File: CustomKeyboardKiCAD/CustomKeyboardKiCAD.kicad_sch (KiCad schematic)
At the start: 4 parts, among them J1 USB_C_Receptacle_USB2.0_16P, U1 nRF52840

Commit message: Progress on schematic
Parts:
- added C1: 10uF, symbol Device:C
- added C2, C3: 4.7uF, symbol Device:C
- added D1: BLUE, symbol Device:D
- added R3: 1K, symbol Device:R
- added R4: 10M, symbol Device:R
- added U2: XC6220B331MR, Package_TO_SOT_SMD:SOT-23-5, symbol Regulator_Linear:XC6220B331MR
- added U4: BQ24075RGTR, BQ24075RGTR:QFN50P300X300X100-17N, symbol BQ24075RGTR:BQ24075RGTR
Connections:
- net GND: now also C1.1, C2.1, R3.2, U2.2 (GND), U4.15 (SYSOFF), U4.17 (EXP), U4.4 (~{CE}), U4.5 (EN2), U4.8 (VSS)
- new net: D1.1 (K), R3.1
- new net BLED: D1.2 (A)
- new net EXT_VCC: C2.2, U2.5 (VOUT)
- new net POWER_PIN: R4.2, U2.3 (CE)
- new net VDDH: C1.2, R4.1, U2.1 (VIN), U4.6 (EN1)
- no-connect marks 3 -> 5
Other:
- moved on the sheet: J1, R1, R2

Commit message: updated the schematic
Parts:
- added C10, C17, C18, C19: 100nF, symbol Device:C
- added C11: 100pF, symbol Device:C
- added C12: 820pF, symbol Device:C
- added C13, C14, C15, C16, C5: 4.7uF, symbol Device:C
- added C20, C4, C8: 1uF, symbol Device:C
- added C21, C22, C6, C7: 12pF, symbol Device:C
- added C23, C24: 1pF, symbol Device:C
- added C25: 1.5pF, symbol Device:C
- added C26, C27, C28: 0.1uF, symbol Device:C
- added C9: 47nF, symbol Device:C
- added D2: ORANGE, symbol Device:LED
- added J2, J3: Conn_01x12_Pin, symbol Connector:Conn_01x12_Pin
- added JP1: Charge Boost, symbol Jumper:Jumper_2_Open
- added L1, L2: 10uH, symbol Device:L
- added L3: 15uH, symbol Device:L
- added L4: 3.9nH, symbol Device:L
- added R5, R6, R7: 10k, symbol Device:R
- added R8: 2k, symbol Device:R
- added R9: 0, symbol Device:R
- added U3, U5, U6: 74HC595, symbol 74xx:74HC595
- added Y1: 32.768kHz FC-12M, symbol Device:Crystal
- added Y2: 32MHz XRCGB32MOODF1H5ORO, symbol Device:Crystal_GND2
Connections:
- net BLED: now also U1.AD10 (P0.15)
- net D+: now also U1.AD6 (D+)
- net D-: now also U1.AD4 (D-)
- net EXT_VCC: now also C26.2, C27.2, C28.2, U3.10 (~{SRCLR}), U3.16 (VCC), U5.10 (~{SRCLR}), U5.16 (VCC), U6.10 (~{SRCLR}), U6.16 (VCC)
- net GND: now also C3.2, U1.B7 (VSS), U1.EP (VSS), C10.2, C11.2, C12.2, C13.2, C14.2, C15.2, C16.2, C17.2, C18.2, C19.2, C20.2, C21.2, C22.2, C24.2, C25.2, C26.1, C27.1, C28.1, C4.2, C5.2, C6.2, C7.2, C8.2, C9.2, R6.1, R7.2, R8.2, U3.13 (~{OE}), U3.8 (GND), U5.13 (~{OE}), U5.8 (GND), U6.13 (~{OE}), U6.8 (GND), Y2.2
- net POWER_PIN: now also U1.AD8 (P0.13)
- net VBUS: now also U1.AD2 (VBUS), U4.13 (IN), C15.1, C4.1
- net VDDH: now also C3.1, U1.Y2 (VDDH), U4.10 (OUT_10), U4.11 (OUT_11), C14.1, R5.2
- net 029: now reaches U1.A10 (AIN5/P0.29)
- net 002: now reaches U1.A12 (AIN0/P0.02)
- net 115: now reaches U1.A14 (P1.15)
- net 113: now reaches U1.A16 (P1.13)
- net VDD_NRF: now reaches U1.A22 (VDD), U1.AD14 (VDD), U1.AD23 (VDD), U1.B1 (VDD), U1.W1 (VDD)
- net VDD_NRF: now also C16.1, C17.1, C18.1, C19.1, C20.1, L1.2
- net at U1.A23 (XC2): now also C21.1, Y2.3
- net 031: now reaches U1.A8 (AIN7/P0.31)
- net SWC: now reaches U1.AA24 (SWDCLK)
- net at U1.AB2 (DCCH): now also L1.1
- net RESET: now reaches U1.AC11 (P0.16)
- net RESET: now also U1.AC13 (P0.18/~{RESET}), U1.AC9 (P0.14)
- net SWD: now reaches U1.AC24 (SWDIO)
- net at U1.AC5 (DECUSB): now also C13.1
- net 017: now reaches U1.AD12 (P0.17)
- net 017: now also U3.12 (RCLK), U5.12 (RCLK), U6.12 (RCLK)
- net 020: now reaches U1.AD16 (P0.20)
- net 022: now reaches U1.AD18 (P0.22)
- net 024: now reaches U1.AD20 (P0.24)
- net 100: now reaches U1.AD22 (TRACEDATA0/P1.00)
- net 111: now reaches U1.B19 (P1.11)
- net at U1.B24 (XC1): now also C22.1, Y2.1
- net at U1.B3 (DCC): now also L2.2
- net at U1.B5 (DEC4): now also U1.E24 (DEC6), C8.1, C9.1, L3.1
- net at U1.C1 (DEC1): now also C10.1
- net at U1.D2 (XL1/P0.00): now also C7.1, Y1.2
- net at U1.D23 (DEC3): now also C11.1
- net at U1.F2 (XL2/P0.01): now also C6.1, Y1.1
- net VSS_PA: now reaches U1.F23 (VSS_PA)
- net VSS_PA: now also C23.2
- net 026: now reaches U1.G1 (P0.26)
- net at U1.H23 (ANT): now also C23.1, L4.2
- net 010: now reaches U1.J24 (NFC2/P0.10)
- net TXD: now reaches U1.L1 (P0.06)
- net 009: now reaches U1.L24 (NFC1/P0.09)
- net 008: now reaches U1.N1 (P0.08)
- net 008: now also U3.11 (SRCLK), U5.11 (SRCLK), U6.11 (SRCLK)
- net at U1.N24 (DEC5): now also C12.1
- net 107: now reaches U1.P23 (P1.07)
- net 106: now reaches U1.R24 (P1.06)
- net 106: now also U3.14 (SER)
- net 011: now reaches U1.T2 (TRACEDATA2/P0.11)
- net 012: now reaches U1.U1 (TRACEDATA1/P0.12)
- net 104: now reaches U1.U24 (P1.04)
- net 102: now reaches U1.W24 (P1.02)
- net 101: now reaches U1.Y23 (P1.01)
- net at U4.1 (TS): now also R6.2
- net at U4.16 (ISET): now also JP1.1 (A), R7.1
- net VBAT: now reaches U4.2 (BAT_2)
- net VBAT: now also U4.3 (BAT_3), C5.1
- net at U4.9 (~{CHG}): now also D2.1 (K)
- new net: D2.2 (A), R5.1
- new net: JP1.2 (B), R8.1
- new net: U3.9 (QH'), U5.14 (SER)
- new net: U5.9 (QH'), U6.14 (SER)
- new net: L2.1, L3.2
- new net: C24.1, L4.1, R9.2
- new net ANTENNA: C25.1, R9.1
- new net COL0: U3.15 (QA)
- new net COL1: U3.1 (QB)
- new net COL10: U5.2 (QC)
- new net COL11: U5.3 (QD)
- new net COL12: U5.4 (QE)
- new net COL13: U5.5 (QF)
- new net COL14: U5.6 (QG)
- new net COL15: U5.7 (QH)
- new net COL16: U6.15 (QA)
- new net COL17: U6.1 (QB)
- new net COL2: U3.2 (QC)
- new net COL3: U3.3 (QD)
- new net COL4: U3.4 (QE)
- new net COL5: U3.5 (QF)
- new net COL6: U3.6 (QG)
- new net COL7: U3.7 (QH)
- new net COL8: U5.15 (QA)
- new net COL9: U5.1 (QB)
- no-connect marks 5 -> 14
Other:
- moved on the sheet: C1, C2, C3, D1, J1, R1, R2, R3, R4, U2, U4

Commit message: major progress on schematic
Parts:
- removed J2, J3: Conn_01x12_Pin, symbol Connector:Conn_01x12_Pin
- added J3: S2B-PH-K-SLFSN, S2B-PH-K-S:CONN_S2B-PH-K-S_JST, symbol S2B-PH-K-S:S2B-PH-K-SLFSN
- added SW91: RotaryEncoder_Switch, Rotary_Encoder:RotaryEncoder_Alps_EC11E-Switch_Vertical_H20mm, symbol Device:RotaryEncoder_Switch
- added U7: nice_nano, nicenano:nice_nano, symbol nicenano:nice_nano
- U3: footprint (none) -> 74HC595D:SOP127P600X175-16N
- U5, U6: footprint (none) -> BQ24075RGTR:QFN50P300X300X100-17N
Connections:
- net 002: now also SW91.S1, U7.18 (AIN0/P0.02)
- net 008: now also U7.2 (RX1/P0.08)
- net 009: now also U7.13 (NFC1/P0.09)
- net 010: now also U7.14 (NFC2/P0.10)
- net 011: now also U7.10 (P0.11)
- net 017: now also U7.5 (P0.17)
- net 020: now also U7.6 (P0.20)
- net 022: now also U7.7 (P0.22)
- net 024: now also U7.8 (P0.24)
- net 029: now also SW91.C, U7.19 (AIN5/P0.29)
- net 031: now also SW91.A, U7.20 (AIN7/P0.31)
- net 100: now also U7.9 (P1.00)
- net 101: now also U7.31 (P1.01)
- net 102: now also U7.32 (P1.02)
- net 104: now also U7.11 (P1.04)
- net 106: now also U7.12 (P1.06)
- net 107: now also U7.33 (P1.07)
- net 111: now also U7.15 (P1.11)
- net 113: now also U7.16 (P1.13)
- net 115: now also U7.17 (P1.15)
- net EXT_VCC: now also U7.21 (VCC)
- net GND: now also J3.2, SW91.B, SW91.S2, U7.23 (GND), U7.3 (GND), U7.4 (GND)
- net RESET: now also U7.22 (RST)
- net VBAT: now also J3.1, U7.24 (BATIN/P0.04)
- net COL18: now reaches U6.2 (QC)
- net TXD renamed 006
- net 006: now also U7.1 (TX0/P0.06)
- no-connect marks 14 -> 31
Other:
- added sheet LEDs (LEDs.kicad_sch)
- added sheet keyboard_matrix (keyboard_matrix.kicad_sch)
- moved on the sheet: C26, C27, C28, U3, U5, U6

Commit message: schematic is generally complete
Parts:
- added J2: Display Connector, Connector_PinHeader_2.54mm:PinHeader_1x04_P2.54mm_Vertical, symbol Connector_Generic:Conn_01x04
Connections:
- net 010: now also J2.4 (Pin_4)
- net 111: now also J2.3 (Pin_3)
- net EXT_VCC: now also J2.2 (Pin_2)
- net GND: now also J2.1 (Pin_1)
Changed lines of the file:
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@@
 	(wire
 		(pts
+			(xy 212.09 290.83) (xy 213.36 290.83)
+		)
+		(stroke
+			(width 0)
+			(type default)
+		)
+	)
+	(wire
+		(pts
 			(xy 281.94 80.01) (xy 281.94 83.82)
 		)
@@
 		)
 	)
+	(global_label "010"
+		(shape input)
+		(at 213.36 298.45 180)
+		(fields_autoplaced yes)
+		(effects
+			(font
+				(size 1.27 1.27)
+			)
+			(justify right)
+		)
+		(property "Intersheetrefs" "${INTERSHEET_REFS}"
+			(at 206.7463 298.45 0)
+			(effects
+				(font
+					(size 1.27 1.27)
+				)
+				(justify right)
+				(hide yes)
+			)
+		)
+	)
 	(global_label "113"
 		(shape input)
@@
 		)
 	)
+	(global_label "EXT_VCC"
+		(shape input)
+		(at 213.36 293.37 180)
+		(fields_autoplaced yes)
+		(effects
+			(font
+				(size 1.27 1.27)
+			)
+			(justify right)
+		)
+		(property "Intersheetrefs" "${INTERSHEET_REFS}"
+			(at 202.4525 293.37 0)
+			(effects
+				(font
+					(size 1.27 1.27)
+				)
+				(justify right)
+				(hide yes)
+			)
+		)
+	)
 	(global_label "008"
 		(shape input)
@@
 		)
 	)
+	(global_label "111"
+		(shape input)
+		(at 213.36 295.91 180)
+		(fields_autoplaced yes)
+		(effects
+			(font
+				(size 1.27 1.27)
+			)
+			(justify right)
+		)
+		(property "Intersheetrefs" "${INTERSHEET_REFS}"
+			(at 206.7463 295.91 0)
+			(effects
+				(font
+					(size 1.27 1.27)
+				)
+				(justify right)
+				(hide yes)
+			)
+		)
+	)
 	(global_label "BLED"
 		(shape input)
@@
 	)
 	(symbol
+		(lib_id "Connector_Generic:Conn_01x04")
+		(at 218.44 293.37 0)
+		(unit 1)
+		(exclude_from_sim no)
+		(in_bom yes)
+		(on_board yes)
+		(dnp no)
+		(fields_autoplaced yes)
+		(property "Reference" "J2"
+			(at 220.98 293.3699 0)
+			(effects
+				(font
+					(size 1.27 1.27)
+				)
+				(justify left)
+			)
+		)
+		(property "Value" "Display Connector"
+			(at 220.98 295.9099 0)
+			(effects
+				(font
+					(size 1.27 1.27)
+				)
+				(justify left)
+			)
+		)
+		(property "Footprint" "Connector_PinHeader_2.54mm:PinHeader_1x04_P2.54mm_Vertical"
+			(at 218.44 293.37 0)
+			(effects
+				(font
+					(size 1.27 1.27)
+				)
+				(hide yes)
+			)
+		)
+		(property "Datasheet" "~"
+			(at 218.44 293.37 0)
+			(effects
+				(font
+					(size 1.27 1.27)
+				)
+				(hide yes)
+			)
+		)
+		(property "Description" "Generic connector, single row, 01x04, script generated (kicad-library-utils/schlib/autogen/connector/)"
+			(at 218.44 293.37 0)
+			(effects
+				(font
+					(size 1.27 1.27)
+				)
+				(hide yes)
+			)
+		)
+		(pin "1"
+		)
+		(pin "2"
+		)
+		(pin "4"
+		)
+		(pin "3"
+		)
+		(instances
+			(project ""
+				(path "/aaa1400c-18c9-4b83-ab7e-c530ca104a6d"
+					(reference "J2")
+					(unit 1)
+				)
+			)
+		)
+	)
+	(symbol
 		(lib_id "power:GND")
 		(at 39.37 153.67 0)
@@
 					(unit 1)
 				)
+			)
+		)
+	)
+	(symbol
+		(lib_id "power:GND")
+		(at 212.09 290.83 270)
+		(unit 1)
+		(exclude_from_sim no)
+		(in_bom yes)
+		(on_board yes)
+		(dnp no)
+		(property "Reference" "#PWR053"
+			(at 205.74 290.83 0)
+			(effects
+				(font
+					(size 1.27 1.27)
+				)
+				(hide yes)
+			)
+		)
+		(property "Value" "GND"
+			(at 207.518 292.354 0)
+			(effects
+				(font
+					(size 1.27 1.27)
+				)
+				(justify right)
+			)
+		)
+		(property "Footprint" ""
+			(at 212.09 290.83 0)
+			(effects
+				(font
+					(size 1.27 1.27)
+				)
+				(hide yes)
+			)
+		)
+		(property "Datasheet" ""
+			(at 212.09 290.83 0)
+			(effects
+				(font
+					(size 1.27 1.27)
+				)
+				(hide yes)
+			)
+		)
+		(property "Description" "Power symbol creates a global label with name \"GND\" , ground"
+			(at 212.09 290.83 0)
+			(effects
+				(font
+					(size 1.27 1.27)
+				)
+				(hide yes)
+			)
+		)
+		(pin "1"
+		)
+		(instances
+			(project "CustomKeyboardKiCAD"
+				(path "/aaa1400c-18c9-4b83-ab7e-c530ca104a6d"
+					(reference "#PWR053")
+					(unit 1)
+				)

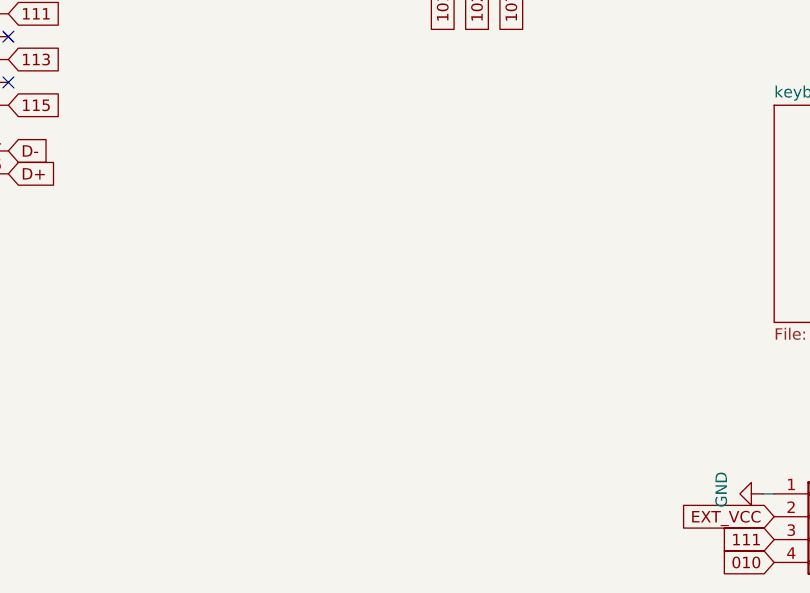
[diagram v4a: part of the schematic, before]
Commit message: major progress on pcb, schematic complete
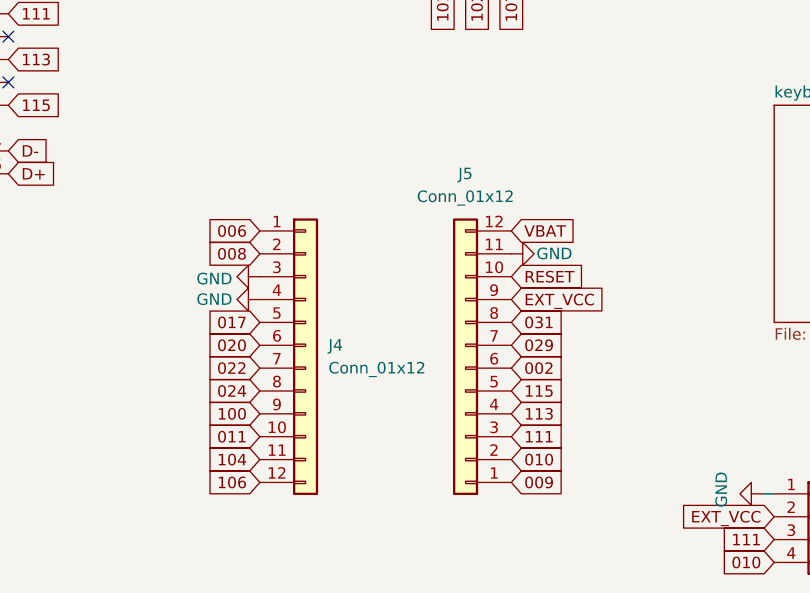
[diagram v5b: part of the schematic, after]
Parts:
- added J4, J5: Conn_01x12, Connector_PinSocket_2.54mm:PinSocket_1x12_P2.54mm_Vertical, symbol Connector_Generic:Conn_01x12
- U5, U6: footprint BQ24075RGTR:QFN50P300X300X100-17N -> 74HC595D:SOP127P600X175-16N
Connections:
- net 002: now also J5.6 (Pin_6)
- net 006: now also J4.1 (Pin_1)
- net 008: now also J4.2 (Pin_2)
- net 009: now also J5.1 (Pin_1)
- net 010: now also J5.2 (Pin_2)
- net 011: now also J4.10 (Pin_10)
- net 017: now also J4.5 (Pin_5)
- net 020: now also J4.6 (Pin_6)
- net 022: now also J4.7 (Pin_7)
- net 024: now also J4.8 (Pin_8)
- net 029: now also J5.7 (Pin_7)
- net 031: now also J5.8 (Pin_8)
- net 100: now also J4.9 (Pin_9)
- net 104: now also J4.11 (Pin_11)
- net 106: now also J4.12 (Pin_12)
- net 111: now also J5.3 (Pin_3)
- net 113: now also J5.4 (Pin_4)
- net 115: now also J5.5 (Pin_5)
- net EXT_VCC: now also J5.9 (Pin_9)
- net GND: now also J4.3 (Pin_3), J4.4 (Pin_4), J5.11 (Pin_11)
- net RESET: now also J5.10 (Pin_10)
- net VBAT: now also J5.12 (Pin_12)

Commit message: more progress on pcb
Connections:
- net COL0: now also U3.7 (QH); no longer U3.15 (QA)
- net COL1: now also U3.6 (QG); no longer U3.1 (QB)
- net COL2: now also U3.5 (QF); no longer U3.2 (QC)
- net COL3: now also U3.4 (QE); no longer U3.3 (QD)
- net COL4: now also U3.3 (QD); no longer U3.4 (QE)
- net COL5: now also U3.2 (QC); no longer U3.5 (QF)
- net COL6: now also U3.1 (QB); no longer U3.6 (QG)
- net COL7: now also U3.15 (QA); no longer U3.7 (QH)

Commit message: pcb complete
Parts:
- added J6: USB_C_Receptacle, symbol Connector:USB_C_Receptacle
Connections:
- net 008: now also U3.12 (RCLK); no longer U3.11 (SRCLK)
- net 017: now also U3.11 (SRCLK); no longer U3.12 (RCLK)
- net COL10: now also U5.7 (QH); no longer U5.2 (QC)
- net COL11: now also U5.6 (QG); no longer U5.3 (QD)
- net COL12: now also U5.5 (QF); no longer U5.4 (QE)
- net COL13: now also U5.4 (QE); no longer U5.5 (QF)
- net COL14: now also U6.2 (QC); no longer U5.6 (QG)
- net COL15: now also U6.1 (QB); no longer U5.7 (QH)
- net COL16: now also U6.3 (QD); no longer U6.15 (QA)
- net COL17: now also U6.4 (QE); no longer U6.1 (QB)
- net COL18: now also U6.5 (QF); no longer U6.2 (QC)
- net VBAT: no longer U7.24 (BATIN/P0.04)
- new net: J6.A1 (GND), J6.A12 (GND), J6.B1 (GND), J6.B12 (GND)
- new net: J6.A4 (VBUS), J6.A9 (VBUS), J6.B4 (VBUS), J6.B9 (VBUS)
- new net V_5VOUTUSB: U7.24 (BATIN/P0.04)
- no-connect marks 31 -> 38
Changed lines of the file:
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@@
 	)
 	(no_connect
-		(at 379.73 228.6)
-	)
-	(no_connect
-		(at 379.73 223.52)
-	)
-	(no_connect
 		(at 128.27 184.15)
 	)
@@
 	)
 	(no_connect
+		(at 321.31 219.71)
+	)
+	(no_connect
 		(at 128.27 245.11)
 	)
@@
 	)
 	(no_connect
-		(at 128.27 232.41)
+		(at 379.73 210.82)
 	)
 	(no_connect
-		(at 379.73 226.06)
+		(at 128.27 232.41)
 	)
 	(no_connect
@@
 	)
 	(no_connect
+		(at 439.42 229.87)
+	)
+	(no_connect
 		(at 128.27 201.93)
 	)
 	(no_connect
+		(at 321.31 217.17)
+	)
+	(no_connect
+		(at 379.73 226.06)
+	)
+	(no_connect
 		(at 128.27 222.25)
 	)
@@
 	)
 	(no_connect
-		(at 379.73 220.98)
-	)
-	(no_connect
 		(at 128.27 140.97)
 	)
@@
 	)
 	(no_connect
-		(at 379.73 218.44)
+		(at 439.42 232.41)
 	)
 	(no_connect
@@
 	)
 	(no_connect
+		(at 439.42 236.22)
+	)
+	(no_connect
+		(at 379.73 228.6)
+	)
+	(no_connect
+		(at 439.42 240.03)
+	)
+	(no_connect
 		(at 232.41 99.06)
 	)
@@
 	)
 	(no_connect
+		(at 439.42 209.55)
+	)
+	(no_connect
+		(at 439.42 204.47)
+	)
+	(no_connect
+		(at 439.42 247.65)
+	)
+	(no_connect
 		(at 77.47 120.65)
 	)
@@
 	(global_label "COL16"
 		(shape input)
-		(at 379.73 210.82 0)
+		(at 379.73 218.44 0)
 		(fields_autoplaced yes)
 		(effects
@@
 		)
 		(property "Intersheetrefs" "${INTERSHEET_REFS}"
-			(at 388.7628 210.82 0)
+			(at 388.7628 218.44 0)
 			(effects
 				(font
@@
 	(global_label "COL18"
 		(shape input)
-		(at 379.73 215.9 0)
+		(at 379.73 223.52 0)
 		(fields_autoplaced yes)
 		(effects
@@
 		)
 		(property "Intersheetrefs" "${INTERSHEET_REFS}"
-			(at 388.7628 215.9 0)
+			(at 388.7628 223.52 0)
 			(effects
 				(font
@@
 	(global_label "COL11"
 		(shape input)
-		(at 321.31 219.71 0)
+		(at 321.31 227.33 0)
 		(fields_autoplaced yes)
 		(effects
@@
 		)
 		(property "Intersheetrefs" "${INTERSHEET_REFS}"
-			(at 330.3428 219.71 0)
+			(at 330.3428 227.33 0)
 			(effects
 				(font
@@
 		)
 	)
-	(global_label "VBAT"
-		(shape input)
-		(at 201.93 193.04 0)
-		(fields_autoplaced yes)
-		(effects
-			(font
-				(size 1.27 1.27)
-			)
-			(justify left)
-		)
-		(property "Intersheetrefs" "${INTERSHEET_REFS}"
-			(at 209.33 193.04 0)
-			(effects
-				(font
-					(size 1.27 1.27)
-				)
-				(justify left)
-				(hide yes)
-			)
-		)
-	)
 	(global_label "VBUS"
 		(shape input)
@@
 	(global_label "COL12"
 		(shape input)
-		(at 321.31 222.25 0)
+		(at 321.31 224.79 0)
 		(fields_autoplaced yes)
 		(effects
@@
 		)
 		(property "Intersheetrefs" "${INTERSHEET_REFS}"
-			(at 330.3428 222.25 0)
+			(at 330.3428 224.79 0)
 			(effects
 				(font
@@
 	(global_label "COL15"
 		(shape input)
-		(at 321.31 229.87 0)
+		(at 379.73 213.36 0)
 		(fields_autoplaced yes)
 		(effects
@@
 		)
 		(property "Intersheetrefs" "${INTERSHEET_REFS}"
-			(at 330.3428 229.87 0)
+			(at 388.7628 213.36 0)
 			(effects
 				(font
@@
 	(global_label "COL17"
 		(shape input)
-		(at 379.73 213.36 0)
+		(at 379.73 220.98 0)
 		(fields_autoplaced yes)
 		(effects
@@
 		)
 		(property "Intersheetrefs" "${INTERSHEET_REFS}"
-			(at 388.7628 213.36 0)
+			(at 388.7628 220.98 0)
 			(effects
 				(font
@@
 	(global_label "008"
 		(shape input)
-		(at 257.81 218.44 180)
+		(at 257.81 226.06 180)
 		(fields_autoplaced yes)
 		(effects
@@
 		)
 		(property "Intersheetrefs" "${INTERSHEET_REFS}"
-			(at 251.1963 218.44 0)
+			(at 251.1963 226.06 0)
 			(effects
 				(font
@@
 		)
 	)
+	(global_label "V_5VOUTUSB"
+		(shape input)
+		(at 201.93 193.04 0)
+		(fields_autoplaced yes)
+		(effects
+			(font
+				(size 1.27 1.27)
+			)
+			(justify left)
+		)
+		(property "Intersheetrefs" "${INTERSHEET_REFS}"
+			(at 216.7081 193.04 0)
+			(effects
+				(font
+					(size 1.27 1.27)
+				)
+				(justify left)
+				(hide yes)
+			)
+		)
+	)
 	(global_label "POWER_PIN"
 		(shape input)
@@
 	(global_label "017"
 		(shape input)
-		(at 257.81 226.06 180)
+		(at 257.81 218.44 180)
 		(fields_autoplaced yes)
 		(effects
@@
 		)
 		(property "Intersheetrefs" "${INTERSHEET_REFS}"
-			(at 251.1963 226.06 0)
+			(at 251.1963 218.44 0)
 			(effects
 				(font
@@
 	(global_label "COL14"
 		(shape input)
-		(at 321.31 227.33 0)
+		(at 379.73 215.9 0)
 		(fields_autoplaced yes)
 		(effects
@@
 		)
 		(property "Intersheetrefs" "${INTERSHEET_REFS}"
-			(at 330.3428 227.33 0)
+			(at 388.7628 215.9 0)
 			(effects
 				(font
@@
 	(global_label "COL10"
 		(shape input)
-		(at 321.31 217.17 0)
+		(at 321.31 229.87 0)
 		(fields_autoplaced yes)
 		(effects
@@
 		)
 		(property "Intersheetrefs" "${INTERSHEET_REFS}"
-			(at 330.3428 217.17 0)
+			(at 330.3428 229.87 0)
 			(effects
 				(font
@@
 	(global_label "COL13"
 		(shape input)
-		(at 321.31 224.79 0)
+		(at 321.31 222.25 0)
 		(fields_autoplaced yes)
 		(effects
@@
 		)
 		(property "Intersheetrefs" "${INTERSHEET_REFS}"
-			(at 330.3428 224.79 0)
+			(at 330.3428 222.25 0)
 			(effects
 				(font
@@
 					(unit 1)
 				)
+			)
+		)
+	)
+	(symbol
+		(lib_id "Connector:USB_C_Receptacle")
+		(at 424.18 214.63 0)
+		(unit 1)
+		(exclude_from_sim no)
+		(in_bom yes)
+		(on_board yes)
+		(dnp no)
+		(fields_autoplaced yes)
+		(property "Reference" "J6"
+			(at 424.18 181.61 0)
+			(effects
+				(font
+					(size 1.27 1.27)
+				)
+			)
+		)
+		(property "Value" "USB_C_Receptacle"
+			(at 424.18 184.15 0)
+			(effects
+				(font
+					(size 1.27 1.27)
+				)
+			)
+		)
+		(property "Footprint" ""
+			(at 427.99 214.63 0)
+			(effects
+				(font
+					(size 1.27 1.27)
+				)
+				(hide yes)
+			)
+		)
+		(property "Datasheet" "https://www.usb.org/sites/default/files/documents/usb_type-c.zip"
+			(at 427.99 214.63 0)
+			(effects
+				(font
+					(size 1.27 1.27)
+				)
+				(hide yes)
+			)
+		)
+		(property "Description" "USB Full-Featured Type-C Receptacle connector"
+			(at 424.18 214.63 0)
+			(effects
+				(font
+					(size 1.27 1.27)
+				)
+				(hide yes)
+			)
+		)
+		(pin "B9"
+		)
+		(pin "S1"
+		)
+		(pin "B7"
+		)
+		(pin "B12"
+		)
+		(pin "B1"
+		)
+		(pin "A9"
+		)
+		(pin "A10"
+		)
+		(pin "A5"
+		)
+		(pin "A8"
+		)
+		(pin "A4"
+		)
+		(pin "A1"
+		)
+		(pin "B4"
+		)
+		(pin "A12"
+		)
+		(pin "B5"
+		)
+		(pin "A7"
+		)
+		(pin "A6"
+		)
+		(pin "B6"
+		)
+		(pin "B10"
+		)
+		(pin "B11"
+		)
+		(pin "A3"
+		)
+		(pin "A2"
+		)
+		(pin "B3"
+		)
+		(pin "A11"
+		)
+		(pin "B2"
+		)
+		(pin "B8"
+		)
+		(instances
+			(project ""
+				(path "/aaa1400c-18c9-4b83-ab7e-c530ca104a6d"
+					(reference "J6")
+					(unit 1)
+				)
